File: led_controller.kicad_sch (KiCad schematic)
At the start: 20 parts, among them SW1 Toggle switch, SW2 Toggle switch, SW3 Toggle switch, SW4 Toggle switch

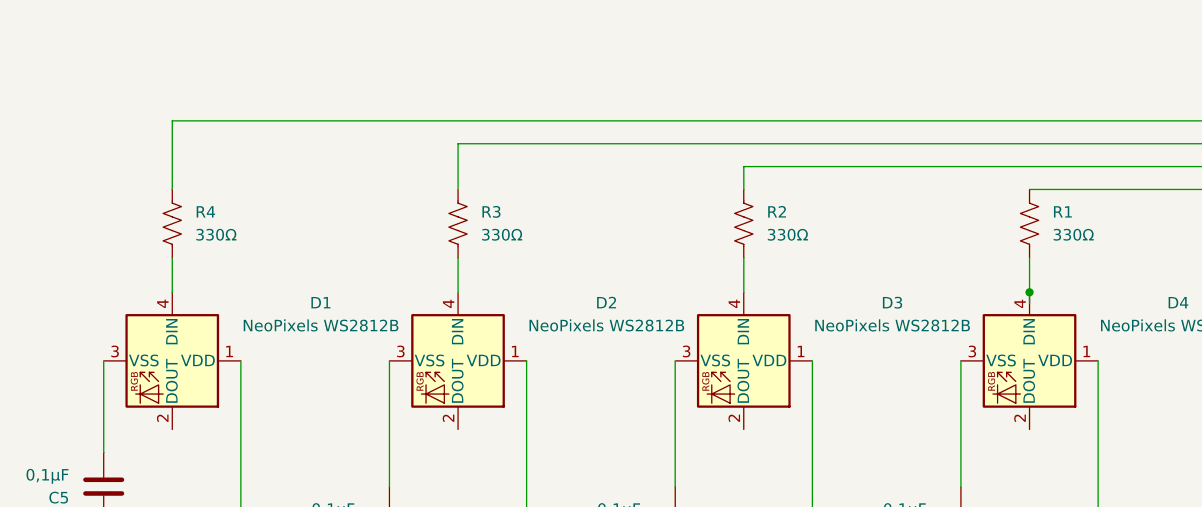
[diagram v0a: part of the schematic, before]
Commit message: change resistors to european notation
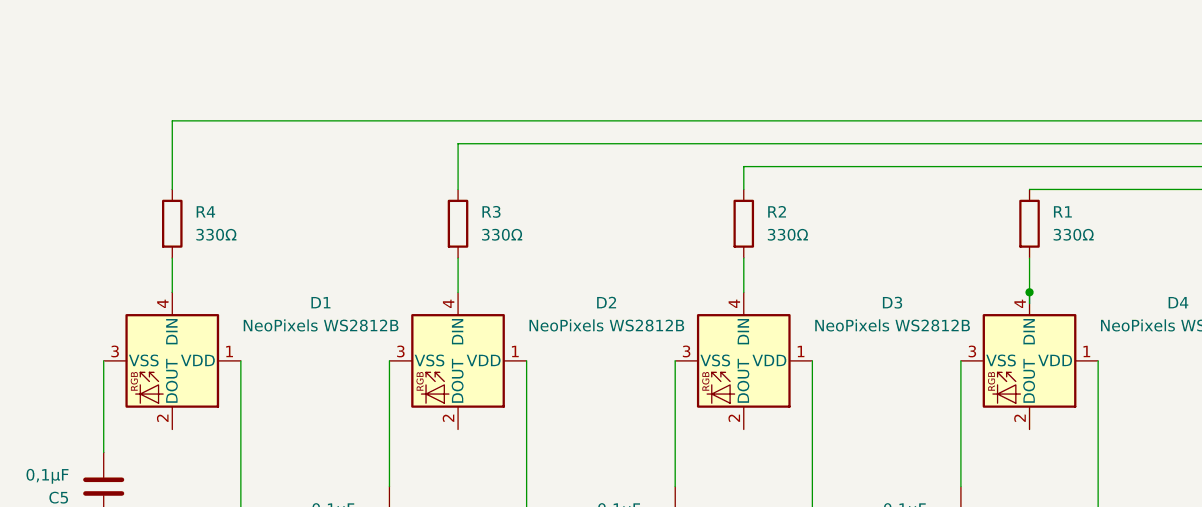
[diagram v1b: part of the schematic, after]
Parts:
- removed R1, R2, R3, R4: 330Ω, symbol Device:R_US
- added R1, R2, R3, R4: 330Ω, symbol Device:R
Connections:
- net at D1.4 (DIN): now also R4.2
- net at A1.5 (D2): now also R4.1
- net at D3.4 (DIN): now also R2.2
- net at A1.7 (D4): now also R2.1
- net at D2.4 (DIN): now also R3.2
- net at D4.4 (DIN): now also R1.2
- net at A1.8 (D5): now also R1.1
- net at A1.6 (D3): now also R3.1
